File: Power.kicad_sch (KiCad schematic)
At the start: 0 parts

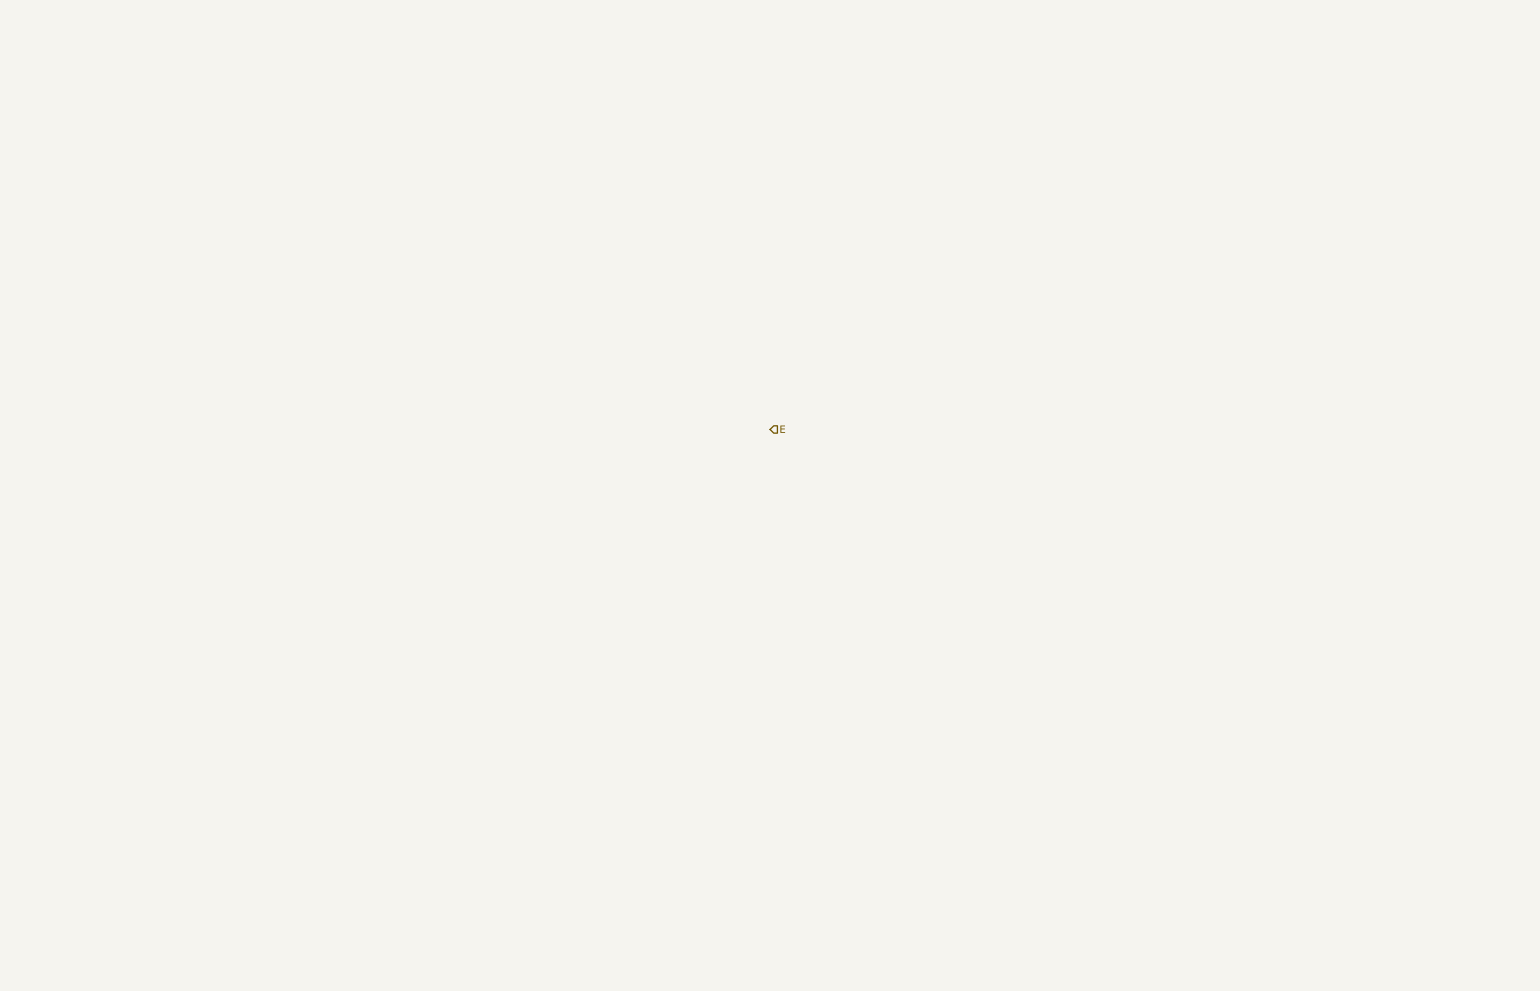
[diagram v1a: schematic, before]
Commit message: Draft 1 - Main components and wiring complete
Connections may be innacurate or violate electrical specs, or perhaps aren't set up "properly".
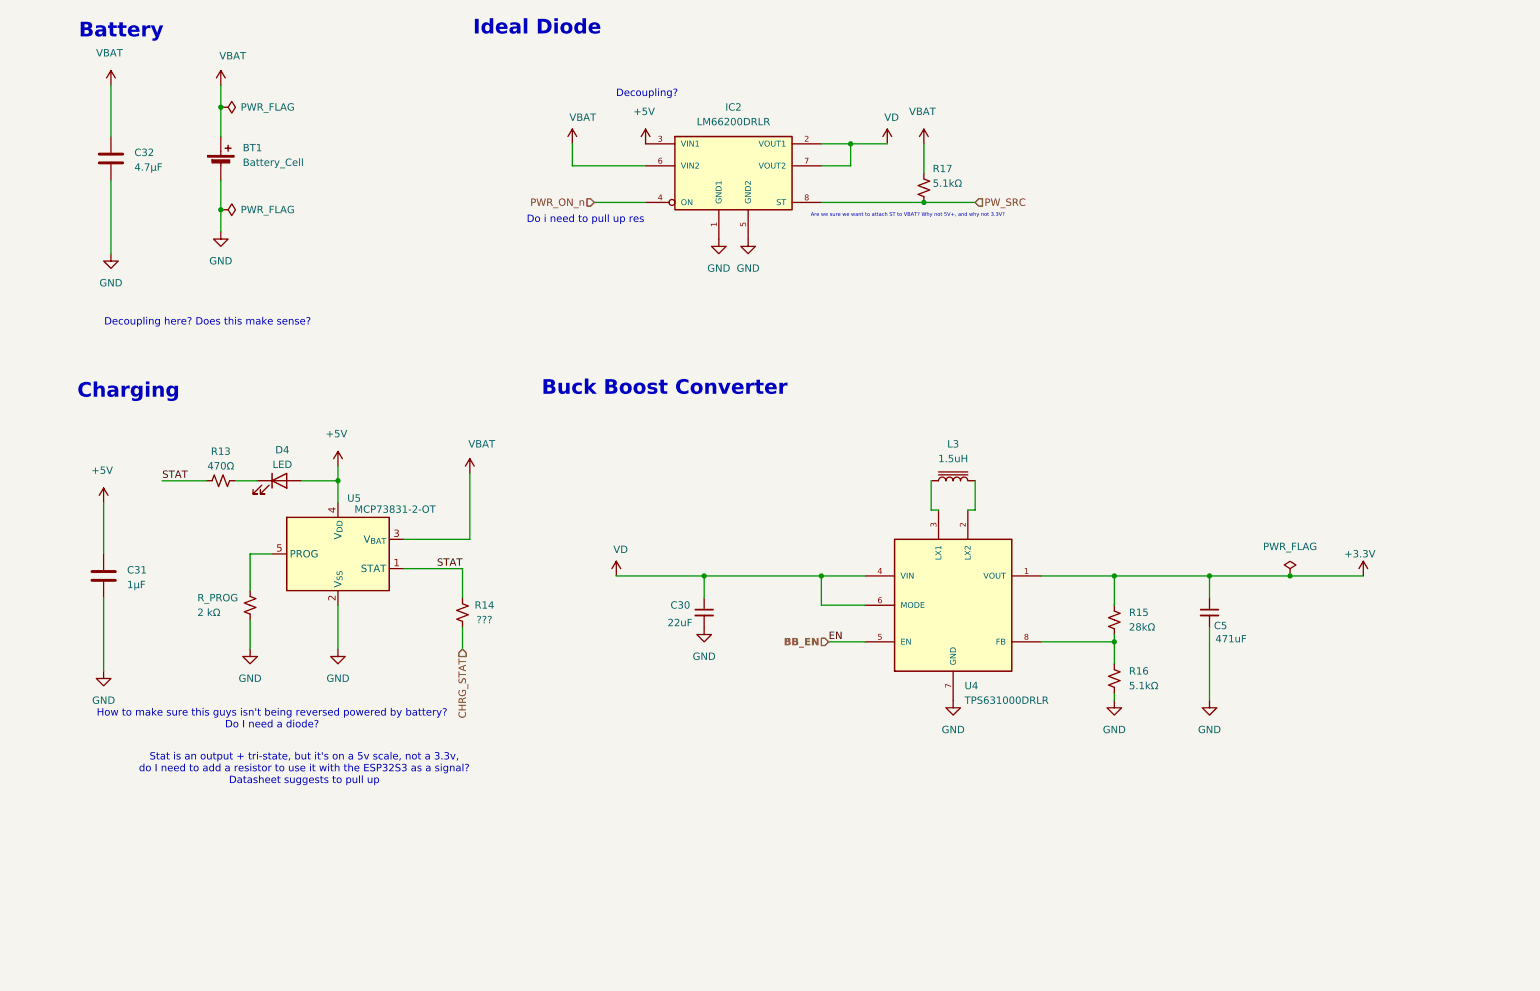
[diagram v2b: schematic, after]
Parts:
- added BT1: Battery_Cell, symbol Device:Battery_Cell
- added C30: 22uF, symbol Device:C_Small
- added C31: 1µF, symbol Device:C
- added C32: 4.7µF, symbol Device:C
- added C5: 471uF, symbol Device:C_Small
- added D4: LED, symbol Device:LED
- added IC2: LM66200DRLR, LM66200DRLR:SOT8, symbol LM66200DRLR:LM66200DRLR
- added L3: 1.5uH, symbol Device:L_Iron
- added R13: 470Ω, symbol Device:R_Small_US
- added R14: ???, symbol Device:R_Small_US
- added R15: 28kΩ, symbol Device:R_Small_US
- added R16, R17: 5.1kΩ, symbol Device:R_Small_US
- added R_PROG: 2 kΩ, symbol Device:R_Small_US
- added U4: TPS631000DRLR, TPS631000DRLR:SOT50P160X60-8N, symbol TPS631000DRLR:TPS631000DRLR
- added U5: MCP73831-2-OT, Package_TO_SOT_SMD:SOT-23-5, symbol Battery_Management:MCP73831-2-OT
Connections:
- new net: L3.2, U4.2 (LX2)
- new net: L3.1, U4.3 (LX1)
- new net: R15.2, R16.1, U4.8 (FB)
- new net: D4.1 (K), R13.2
- new net: R_PROG.1, U5.5 (PROG)
- new net +3.3V: C5.1, R15.1, U4.1 (VOUT)
- new net +5V: C31.2, D4.2 (A), IC2.3 (VIN1), U5.4 (V_{DD})
- new net BB_EN: U4.5 (EN)
- new net CHRG_STAT: R14.2
- new net GND: BT1.2 (-), C30.2, C31.1, C32.1, C5.2, IC2.1 (GND1), IC2.5 (GND2), R16.2, R_PROG.2, U4.7 (GND), U5.2 (V_{SS})
- new net PWR_ON_n: IC2.4 (ON)
- new net PW_SRC: IC2.8 (ST), R17.2
- new net STAT: R13.1, R14.1, U5.1 (STAT)
- new net VBAT: BT1.1 (+), C32.2, IC2.6 (VIN2), R17.1, U5.3 (V_{BAT})
- new net VD: C30.1, IC2.2 (VOUT1), IC2.7 (VOUT2), U4.4 (VIN), U4.6 (MODE)
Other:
- note added: "Are we sure we want to attach ST to VBAT? Why not 5V+, and why not 3.3V?"
- note added: "Battery"
- note added: "Buck Boost Converter"
- note added: "Charging"
- note added: "Decoupling here? Does this make sense?"
- note added: "Decoupling?"
- note added: "Do i need to pull up res"
- note added: "How to make sure this guys isn't being reversed powered by battery? Do I need a diode?"
- note added: "Ideal Diode"
- note added: "Stat is an output + tri-state, but it's on a 5v scale, not a 3.3v, do I need to add a resistor to use it with the ESP32S3 as a signal? Datasheet suggests to pull up"

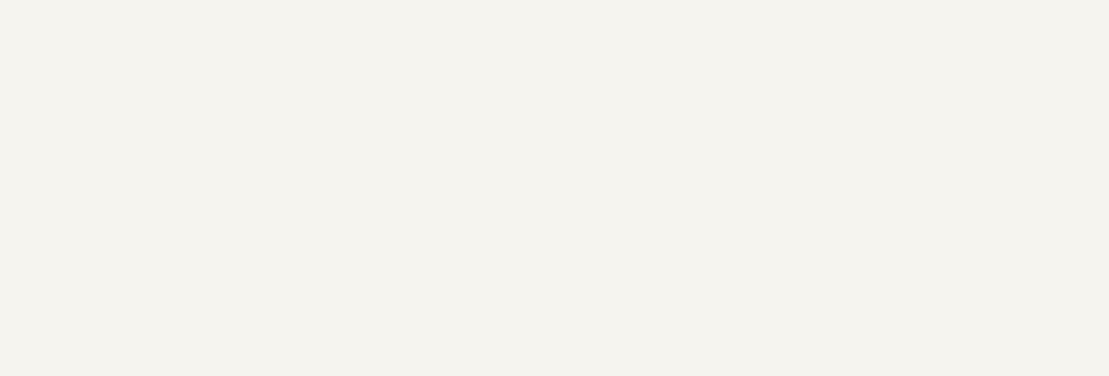
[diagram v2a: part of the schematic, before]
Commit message: Added missing datasheets.
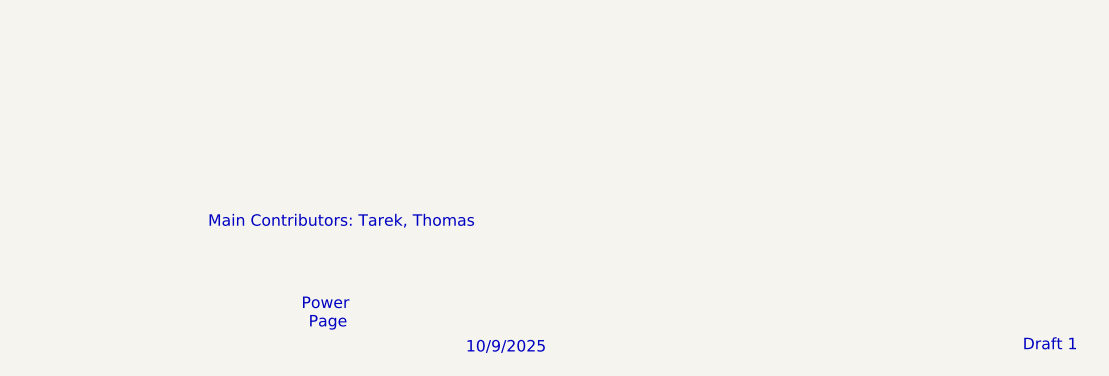
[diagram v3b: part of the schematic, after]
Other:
- note added: "10/9/2025"
- note added: "Draft 1"
- note added: "Main Contributors: Tarek, Thomas"
- note added: "Power Page"
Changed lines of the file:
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@@
+		)
+	)
+	(text "Power\n Page"
+		(exclude_from_sim no)
+		(at 192.532 189.484 0)
+		(effects
+			(font
+				(size 1.27 1.27)
+			)
 		)
 	)
@@
 		)
 	)
+	(text "Main Contributors: Tarek, Thomas"
+		(exclude_from_sim no)
+		(at 194.31 179.324 0)
+		(effects
+			(font
+				(size 1.27 1.27)
+			)
+		)
+	)
 	(text "Do i need to pull up res"
 		(exclude_from_sim no)
@@
 		)
 	)
+	(text "10/9/2025"
+		(exclude_from_sim no)
+		(at 212.598 193.294 0)
+		(effects
+			(font
+				(size 1.27 1.27)
+			)
+		)
+	)
 	(text "Decoupling here? Does this make sense?"
 		(exclude_from_sim no)
@@
 				(thickness 0.508)
 				(bold yes)
+			)
+		)
+	)
+	(text "Draft 1"
+		(exclude_from_sim no)
+		(at 273.05 193.04 0)
+		(effects
+			(font
+				(size 1.27 1.27)
 			)
 		)
@@
 			)
 		)
-		(property "Datasheet" ""
+		(property "Datasheet" "https://www.ti.com/lit/ds/symlink/tps631000.pdf"
 			(at 177.8 130.81 0)
 			(effects

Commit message: Added PMOS to battery + power flags
Still missing values for a lot of components
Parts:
- added D5: ???, symbol Device:D_Zener
- added Q1: PMOS ???, symbol Simulation_SPICE:PMOS
- added R18: ???Ω, symbol Device:R_Small_US
- C5: value 471uF -> 47uF
- renumbered R_PROG to R19
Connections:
- net GND: now also R18.1
- net VBAT: now also D5.1 (K), Q1.3 (S); no longer BT1.1 (+)
- net +5V renamed USB_V
- net VD renamed 3V - 5V
- new net: BT1.1 (+), Q1.1 (D)
- new net: D5.2 (A), Q1.2 (G), R18.2
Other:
- moved on the sheet: IC2, R17

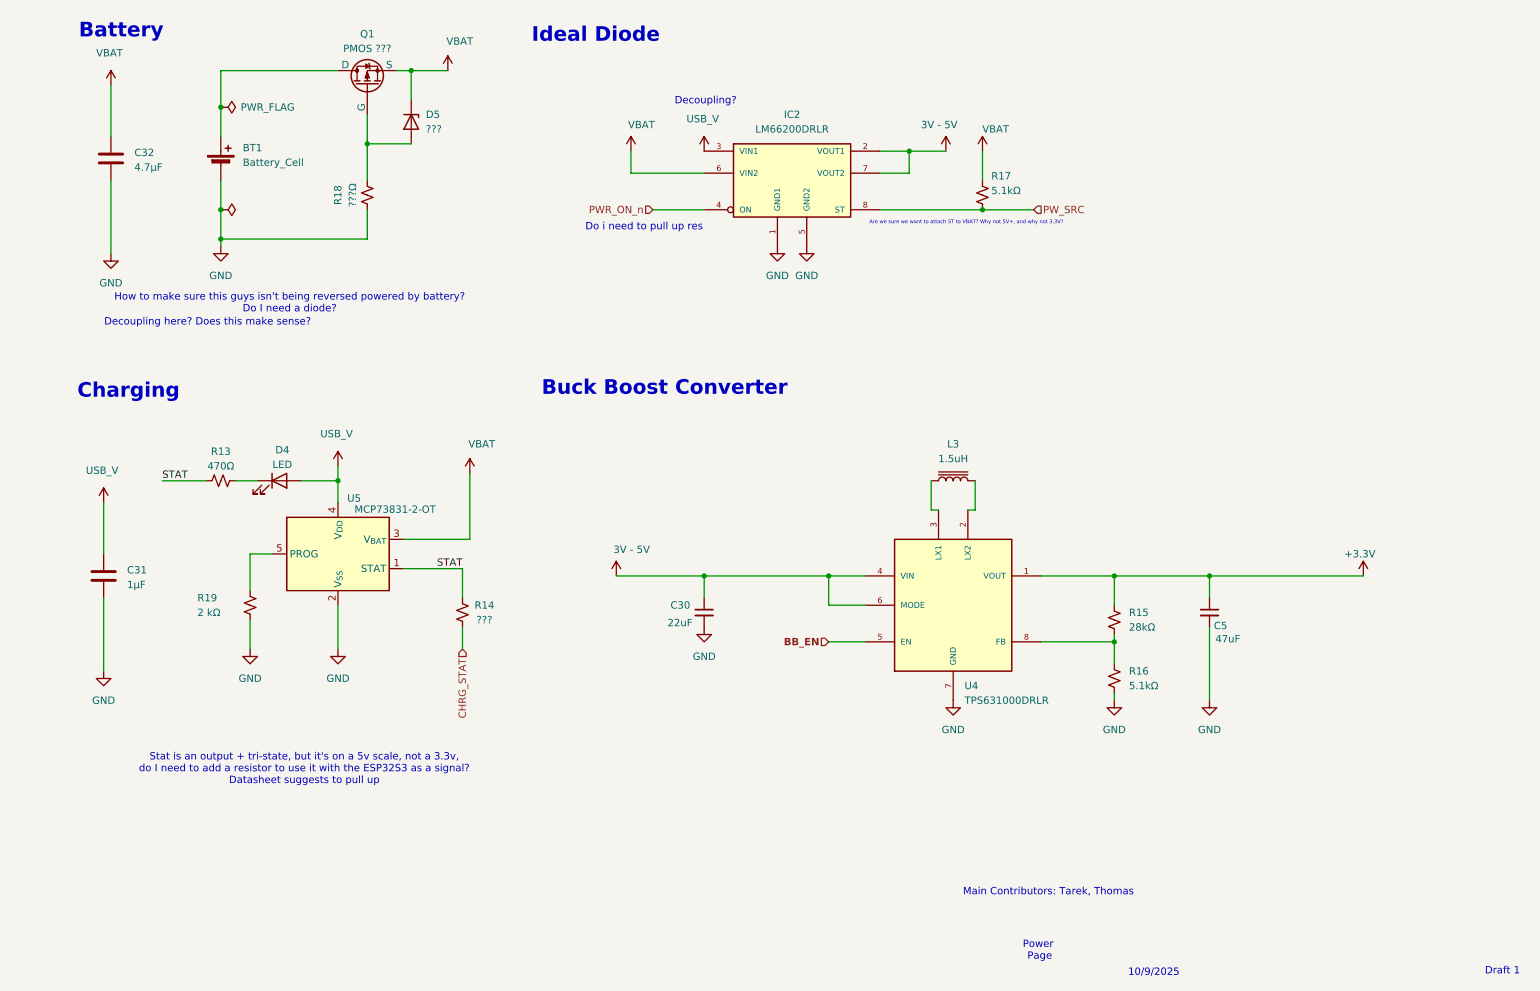
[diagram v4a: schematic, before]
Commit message: Draft 2: Protection circuitry and fixed I/O signals
Still missing PMOS spec for reverse polarity battery protection. Added TVS to USB, voltage divided certain output signals from ICs into ESP GPIO. Checked some component values.
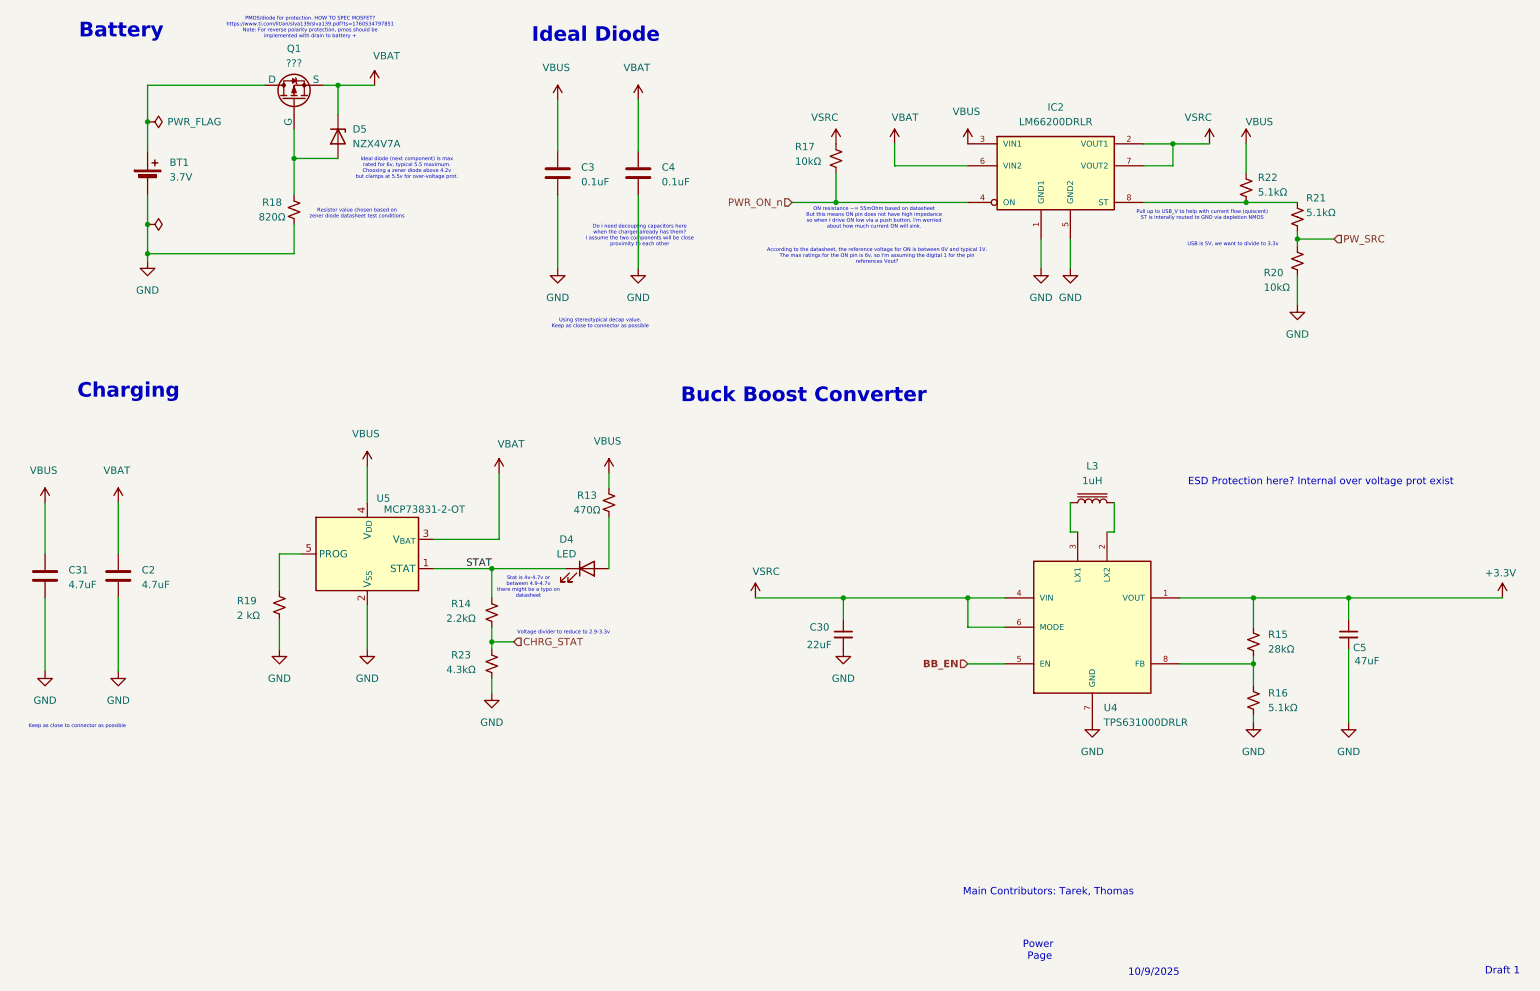
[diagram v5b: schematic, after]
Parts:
- removed C32: 4.7µF, symbol Device:C
- added C2: 4.7uF, symbol Device:C
- added C3, C4: 0.1uF, symbol Device:C
- added R20: 10kΩ, symbol Device:R_Small_US
- added R21, R22: 5.1kΩ, symbol Device:R_Small_US
- added R23: 4.3kΩ, symbol Device:R_Small_US
- BT1: value Battery_Cell -> 3.7V
- C31: value 1µF -> 4.7uF
- D5: value ??? -> NZX4V7A; footprint (none) -> https://assets.nexperia.com/documents/data-sheet/NZX_SER.pdf
- L3: value 1.5uH -> 1uH
- Q1: value PMOS ??? -> ???
- R14: value ??? -> 2.2kΩ
- R17: value 5.1kΩ -> 10kΩ
- R18: value ???Ω -> 820Ω
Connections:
- net CHRG_STAT: now also R23.1
- net GND: now also C2.1, C3.1, C4.1, R20.1, R23.2
- net PWR_ON_n: now also R17.2
- net PW_SRC: now also R20.2, R21.2; no longer IC2.8 (ST), R17.2
- net STAT: now also D4.1 (K); no longer R13.1
- net VBAT: now also C2.2, C4.2; no longer R17.1
- net VBUS: now reaches R13.2
- net VBUS: now also C31.2, IC2.3 (VIN1), U5.4 (V_{DD}), C3.2, R22.1; no longer D4.1 (K)
- net 3V - 5V renamed VSRC
- net VSRC: now also R17.1
- removed net USB_V: C31.2, D4.2 (A), IC2.3 (VIN1), U5.4 (V_{DD})
- new net: D4.2 (A), R13.1
- new net: IC2.8 (ST), R21.1, R22.2
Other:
- note added: "According to the datasheet, the reference voltage for ON is between 0V and typical 1V. The max ratings for the ON pin is 6v, so I'm assuming the digital 1 for the pin references Vout?"
- note added: "Do i need decoupling capacitors here when the charger already has them? I assume the two components will be close proximity to each other"
- note added: "ESD Protection here? Internal over voltage prot exist"
- note added: "Ideal diode (next component) is max rated for 6v, typical 5.5 maximum. Choosing a zener diode above 4.2v but clamps at 5.5v for over-voltage prot."
- note added: "Keep as close to connector as possible"
- note added: "ON resistance ~= 55mOhm based on datasheet But this means ON pin does not have high impedance so when I drive ON low via a push button, I'm worried about how much current ON will sink."
- note added: "PMOS/diode for protection. HOW TO SPEC MOSFET? https://www.ti.com/lit/an/slva139/slva139.pdf?ts=1760534797851 Note: For reverse polarity protection, pmos should be implemented with drain to battery +"
- note added: "Pull up to USB_V to help with current flow (quiscent) ST is interally routed to GND via depletion NMOS"
- note added: "Resistor value chosen based on zener diode datasheet test conditions"
- note added: "Stat is 4v-4.7v or between 4.9-4.7v there might be a typo on datasheet"
- note added: "USB is 5V, we want to divide to 3.3v"
- note added: "Using stereotypical decap value. Keep as close to connector as possible"
- note added: "Voltage divider to reduce to 2.9-3.3v"
- note removed: "Are we sure we want to attach ST to VBAT? Why not 5V+, and why not 3.3V?"
- note removed: "Decoupling here? Does this make sense?"
- note removed: "Decoupling?"
- note removed: "Do i need to pull up res"
- note removed: "How to make sure this guys isn't being reversed powered by battery? Do I need a diode?"
- note removed: "Stat is an output + tri-state, but it's on a 5v scale, not a 3.3v, do I need to add a resistor to use it with the ESP32S3 as a signal? Datasheet suggests to pull up"
- moved on the sheet: BT1, C30, C31, C5, D5, IC2, L3, Q1, R13, R14, R15, R16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
